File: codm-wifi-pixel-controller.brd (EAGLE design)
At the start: 59 x 25.5 mm, 24 parts, among them U1 ESP-WROOM-02, U2 AP2112K, U3 SN74AHCT125D

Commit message: development version 0.7
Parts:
- removed R3: 10k, rcl:R0805
- added C7, C8, C9: 2.2uF, rcl:C0603
- added U4: REG710NA-5/250, REG710NA-5_250:SOT95P280X145-6N
- C1, C2, C3, C4: device rcl:C0805 -> rcl:C0603
- C5: value 1u -> 1uF; device rcl:C0805 -> rcl:C0603
- C6: value 1u -> 2.2uF; device rcl:C0805 -> rcl:C0603
- F1: value 8V 500mA -> 24V 500mA (507-1803-1-ND)
- R1, R2: device rcl:R0805 -> rcl:R0603
- U2: value AP2112K -> TLV76733DRVR; device SparkFun-IC-Power:SOT23-5 -> TLV76733DRVR:SON65P200X200X80-7N
- moved C6 8.12 mm to (41.0, 3.00)
- moved C4 6.80 mm to (36.0, 17.2), turned to 0 degrees
- moved C5 6.73 mm to (47.0, 3.00), turned to 270 degrees
- moved RESET 2.07 mm to (32.3, 2.60)
- moved U$1 2.00 mm to (31.6, 21.8)
- moved U3 1.41 mm to (36.0, 11.5)
- moved D1 1.14 mm to (49.9, 9.60)
- moved JP1 1.00 mm to (20.8, 2.84)
- moved R1 1.00 mm to (41.4, 10.2)
- moved U$100 1.00 mm to (27.0, 9.50)
- moved U$2 1.00 mm to (8.00, 21.4)
- moved U1 1.00 mm to (20.8, 13.2)
- moved U2 0.71 mm to (44.0, 3.00)
- moved F1 0.64 mm to (49.9, 7.00)
- moved C3 0.57 mm to (8.60, 12.9)
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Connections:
- new net N$3: C9.2, U4.4
- new net VCCF: C5.1, D1.C, F1.2, U2.4, U2.6
- net +3V3: now also C6.2, C7.2, U2.1, U2.2, U4.3, U4.5; no longer C5.2, U2.5
- net +5V: now also C8.2, U4.1; no longer C6.2, D1.C, F1.2, R3.1, U2.1
- net GND: now also C5.2, C7.1, C8.1, U2.3, U2.5, U2.7, U4.2; no longer C5.1, U2.2
- net N$1: now also C9.1, U4.6; no longer R3.2, U2.3
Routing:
- net +5V: track 27.8 -> 10.7 mm
- net +3V3: track 60.9 -> 74.0 mm, vias 3 -> 9
- net VCCF: track 0.00 -> 7.05 mm, vias 0 -> 4
- net N$3: track 0.00 -> 5.27 mm
- net CLK-5V: track 23.1 -> 24.6 mm
- net DATA-5V: track 4.03 -> 3.13 mm
- net CHIPEN: track 13.6 -> 14.3 mm
- net CLK: track 32.4 -> 33.2 mm
- net N$1: track 2.35 -> 3.03 mm
- net STATLED: track 8.52 -> 7.93 mm
- net GND: vias 2 -> 15
- added copper zone on layer 1, net +3V3
- added copper zone on layer 16, net GND
- added copper zone on layer 1, net VCCF
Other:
- board text added: "4.7-16V"
- board text added: "90060-0.7"
- board text added: "VCC"
- board text added: "Wi-Fi Pixel Controller V0.7 codm.de 2021, CC-BY-NC-SA"
- board text added: "codm.de, 2021"
- board text removed: "+5V"
- board text removed: "90060-0.6"
- board text removed: "Wi-Fi Pixel Controller V0.6 codm.de 2020, CC-BY-NC-SA"
- board text removed: "codm.de, 2020"

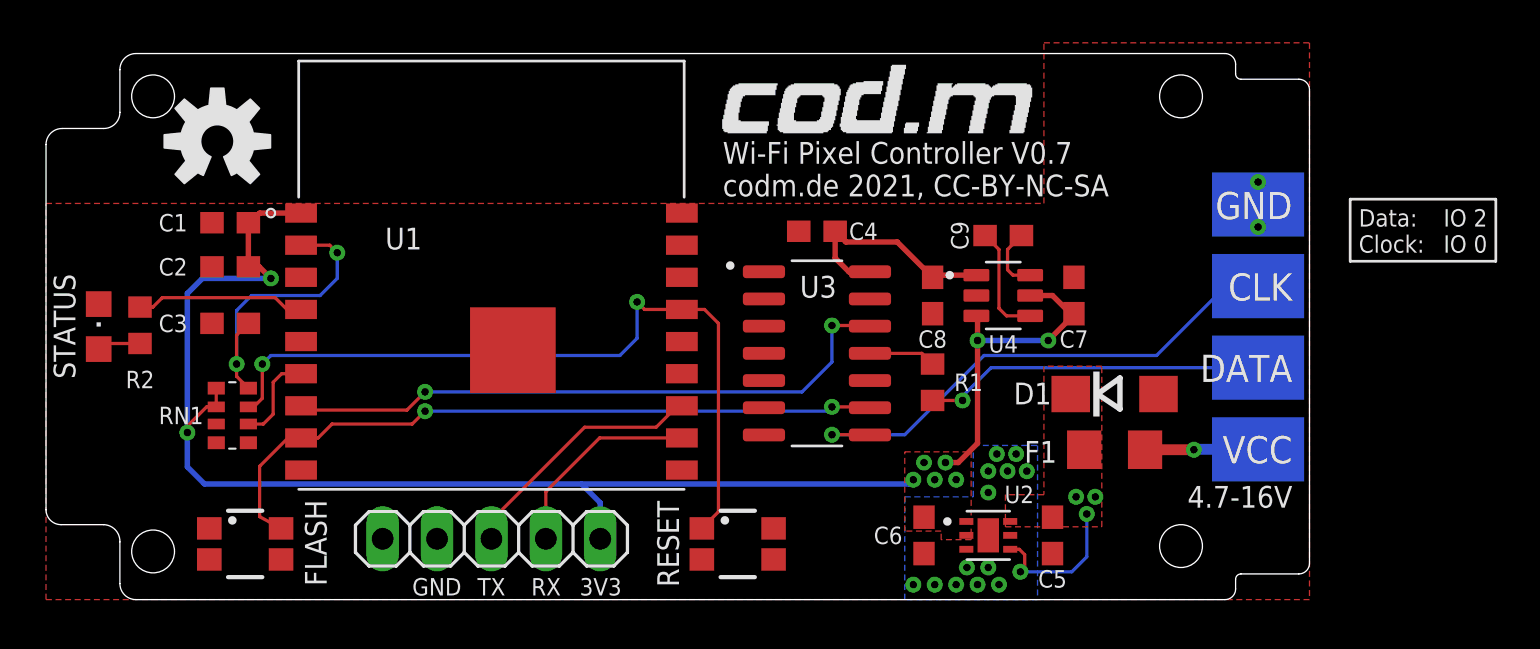
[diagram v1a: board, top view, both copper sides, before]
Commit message: version with TLV767 and bigger thermal via/planes
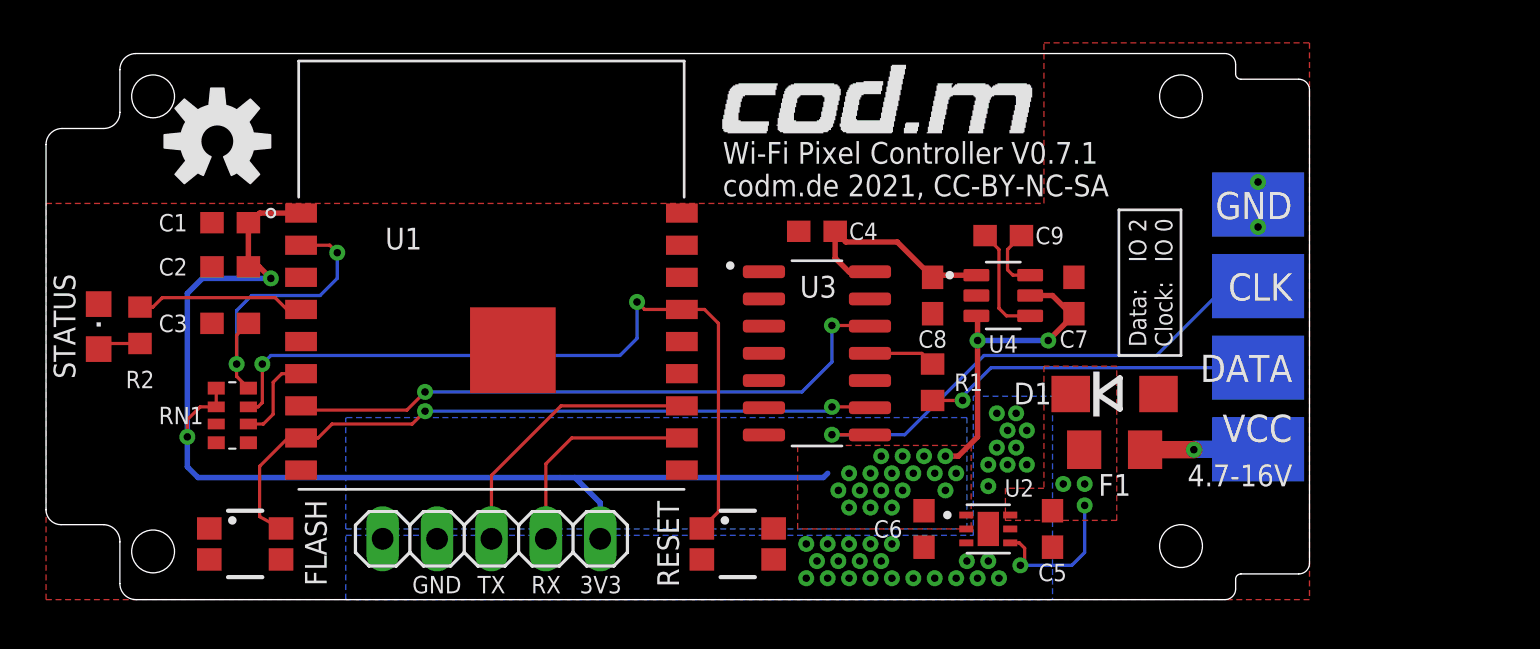
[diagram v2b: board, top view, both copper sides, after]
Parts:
- moved C5 0.30 mm to (47.0, 3.30)
- moved C6 0.30 mm to (41.0, 3.30)
- moved U2 0.30 mm to (44.0, 3.30)
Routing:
- net +3V3: track 74.0 -> 70.3 mm, vias 9 -> 22
- net TXD: track 12.0 -> 13.2 mm
- net RXD: track 9.59 -> 10.4 mm
- net GND: vias 15 -> 33
- added copper zone on layer 16, net +3V3
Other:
- board text added: "90060-0.7.1"
- board text added: "Wi-Fi Pixel Controller V0.7.1 codm.de 2021, CC-BY-NC-SA"
- board text removed: "90060-0.7"
- board text removed: "Wi-Fi Pixel Controller V0.7 codm.de 2021, CC-BY-NC-SA"

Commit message: prototype 0.7.2
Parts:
- added C10: 100n, rcl:C0603K
- added EN-2ND: (no value), jumper:SJ
- added R3: 330, rcl:R0603
- added TP1, TP2, TP3, TP4, TP5, TP6, TP7, TP8, TP9: PTR1TP14R, testpad:TP14R
- C1, C2, C3, C7, C8, C9: device rcl:C0603 -> rcl:C0603K
- C4: value 100n -> 10u; device rcl:C0603 -> rcl:C0805
- C5: value 1uF -> 10uF/16V; device rcl:C0603 -> rcl:C0805K
- C6: value 2.2uF -> 100n; device rcl:C0603 -> rcl:C0603K
- U2: value TLV76733DRVR -> TLV1117LV33DCYR; device TLV76733DRVR:SON65P200X200X80-7N -> TLV1117LV33DCYR:VREG_TLV1117LV33DCYR
- moved U$102 25.3 mm to (9.40, 19.5)
- moved U$100 24.7 mm to (50.3, 1.20)
- moved C4 9.20 mm to (34.1, 8.20)
- moved C6 7.48 mm to (34.1, 6.20), turned to 0 degrees
- moved C8 5.66 mm to (47.0, 15.0)
- moved U4 5.46 mm to (50.1, 15.0)
- moved C9 5.42 mm to (50.1, 17.5)
- moved C7 5.26 mm to (53.2, 15.0)
- moved R1 5.14 mm to (42.4, 15.2), turned to 180 degrees
- moved U3 3.10 mm to (35.9, 14.6), turned to 270 degrees
- moved U2 3.08 mm to (41.5, 5.10), turned to 180 degrees
- moved C5 1.87 mm to (47.5, 5.10)
- moved D1 1.17 mm to (50.3, 10.7)
- moved F1 1.17 mm to (50.3, 8.10)
- moved U$2 0.92 mm to (8.70, 20.8)
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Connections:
- net CLK-5V renamed CLK1-5V
- net DATA-5V renamed DATA1-5V
- new net CLK2-5V: TP9.TP, U3.3
- new net DATA2-5V: R3.2, U3.6
- new net DATA2-5VR: R3.1, TP8.TP
- new net IO13: TP5.TP, U1.5
- new net IO14: TP6.TP, U1.3
- new net IO16: U1.17, U3.2
- new net IO4: TP3.TP, U1.10
- new net IO5: TP4.TP, U1.14
- new net N$4: EN-2ND.2, U3.1, U3.4
- net +3V3: now also C4.2, TP2.TP, U2.4; no longer U2.1
- net +5V: now also C10.2; no longer C4.2
- net GND: now also C10.1, EN-2ND.1, TP1.TP, TP7.TP, U2.1; no longer U2.3, U2.5, U2.7, U3.1, U3.4
- net TXD: now also U3.5
- net VCCF: now also U2.3; no longer U2.4, U2.6
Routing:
- net +3V3: track 70.3 -> 37.0 mm, vias 22 -> 64
- net CLK2-5V: track 0.00 -> 16.1 mm, vias 0 -> 1
- net IO16: track 0.00 -> 14.6 mm, vias 0 -> 2
- net N$4: track 0.00 -> 12.7 mm, vias 0 -> 1
- net TXD: track 13.2 -> 24.5 mm
- net DATA2-5VR: track 0.00 -> 10.2 mm, vias 0 -> 1
- net DATA2-5V: track 0.00 -> 9.89 mm
- net IO4: track 0.00 -> 8.13 mm, vias 0 -> 1
- net GND: track 2.10 -> 9.44 mm, vias 33 -> 4
- net IO14: track 0.00 -> 4.69 mm, vias 0 -> 1
- net DATA1-5V: track 3.13 -> 7.80 mm
- net IO5: track 0.00 -> 4.12 mm, vias 0 -> 1
- net IO13: track 0.00 -> 4.03 mm, vias 0 -> 1
- net CLK: track 33.2 -> 30.3 mm
- net DATA-5VR: track 16.0 -> 18.7 mm
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- removed copper zone on layer 16, net GND
- removed copper zone on layer 1, net VCCF
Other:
- board text added: "3.3V"
- board text added: "90060-0.7.2"
- board text added: "Clock-2 (IO16)"
- board text added: "Data-2 (IO1)"
- board text added: "IO13"
- board text added: "IO14"
- board text added: "IO4"
- board text added: "IO5"
- board text added: "Wi-Fi Pixel Controller V0.7.2 codm.de 2021, CC-BY-NC-SA"
- board text removed: "90060-0.7.1"
- board text removed: "Thank you for the idea, Dennis. www.unser-smartes-zuhause.de"
- board text removed: "Wi-Fi Pixel Controller V0.7.1 codm.de 2021, CC-BY-NC-SA"

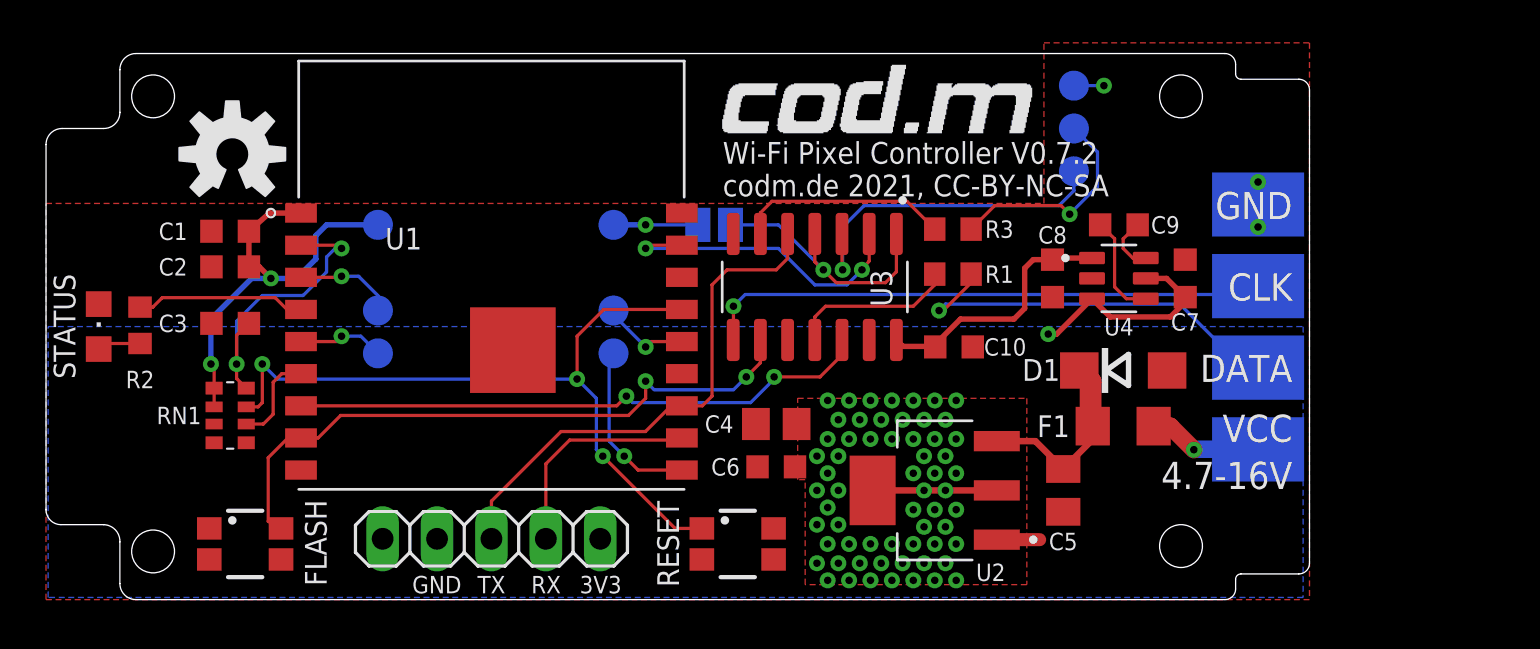
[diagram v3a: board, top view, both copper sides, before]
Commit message: V0.7.3 - forgot reverse polarity protection
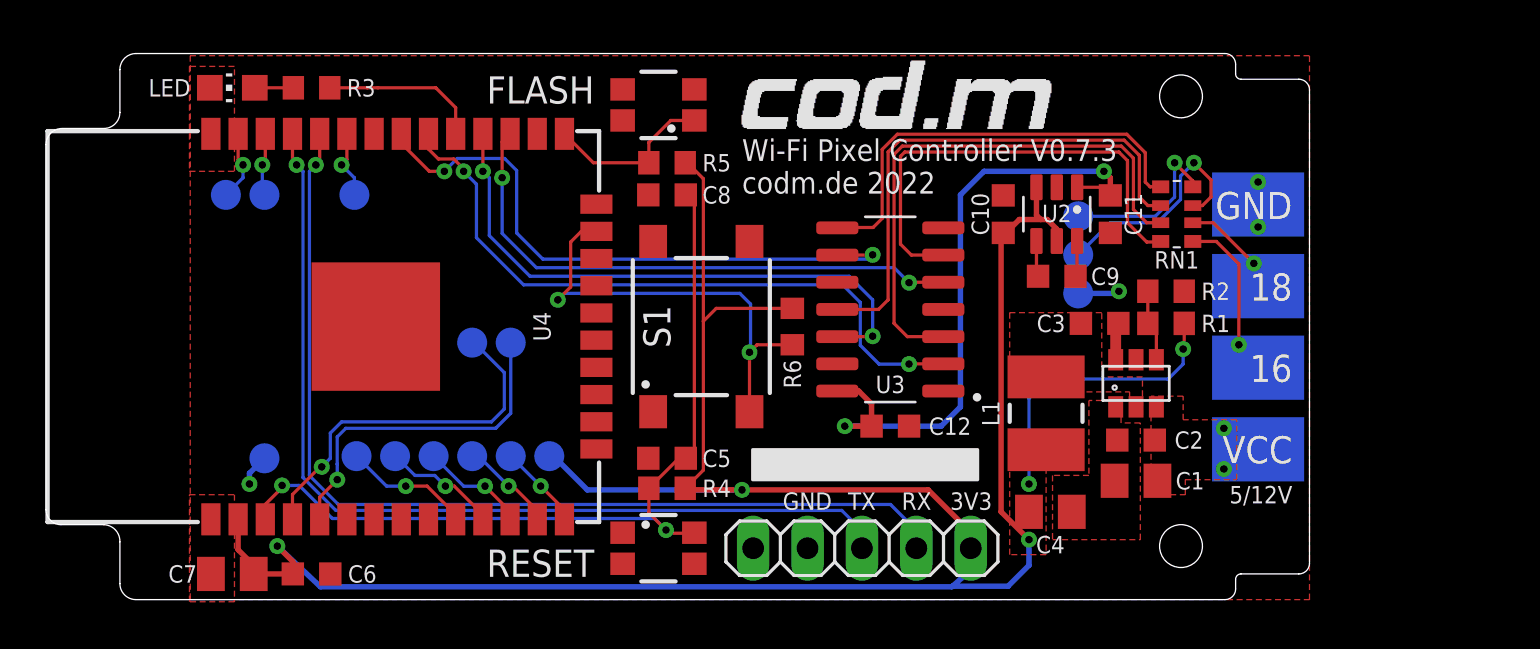
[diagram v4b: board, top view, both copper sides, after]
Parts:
- removed D1: SK34A, diode:DO214AC
- removed EN-2ND: (no value), jumper:SJ
- removed F1: 24V 500mA (507-1803-1-ND), adafruit:R1206
- removed STATUS: (no value), led:CHIPLED_0805
- removed U$2: (no value), SparkFun-Aesthetics:OSHW-LOGO-M
- added C11: 2.2uF, rcl:C0603K
- added C12: 100n, rcl:C0603K
- added L1: 3.3uH, Eagle_WE-LQ (rev19a):WE-LQ_1812
- added LED: 150080RS75000, led:CHIP-LED0805
- added R4, R5, R6: 10k, rcl:R0603
- added S1: 430182070816, Eagle_WS-TASV (rev21c):430182070816
- added TP10, TP11, TP12, TP13, TP14, TP15: PTR1TP14R, testpad:TP14R
- C1: value 100n -> 10u; device rcl:C0603K -> rcl:C0805K
- C10: value 100n -> 2.2uF
- C2: value 10µ -> 100n
- C4: value 10u -> 22uF/6.3V/20%; device rcl:C0805 -> rcl:C0805K
- C5: value 10uF/16V -> 1u; device rcl:C0805K -> rcl:C0603K
- C7: value 2.2uF -> 22uF/6.3V/20%; device rcl:C0603K -> rcl:C0805K
- C8: value 2.2uF -> 100n
- R1: value 330 -> 69k8
- R2: value 2k7 -> 22k1
- R3: value 330 -> 2k7
- RN1: value 10k -> 330
- U1: value ESP-WROOM-02 -> AP62XXX-TSOT26; device ESP-WROOM-02:MODULE_ESP-WROOM-02 -> codm:AP62XXX-TSOT26
- U2: value TLV1117LV33DCYR -> REG710NA-5/250; device TLV1117LV33DCYR:VREG_TLV1117LV33DCYR -> REG710NA-5_250:SOT95P280X145-6N
- U4: value REG710NA-5/250 -> ESP-WROOM-32; device REG710NA-5_250:SOT95P280X145-6N -> esp32:ESP-WROOM-32
- moved R2 47.9 mm to (52.3, 14.4), turned to 0 degrees
- moved C7 46.6 mm to (8.70, 1.20), turned to 0 degrees
- moved RN1 45.2 mm to (52.8, 18.0)
- moved C1 43.9 mm to (50.9, 5.55), turned to 0 degrees
- moved C2 43.1 mm to (50.9, 7.45)
- moved C3 40.6 mm to (49.2, 12.9)
- moved U4 34.8 mm to (15.4, 12.8), turned to 180 degrees
- moved R3 30.7 mm to (12.4, 23.9), turned to 0 degrees
- moved U1 30.3 mm to (50.9, 10.1), turned to 90 degrees
- moved FLASH 28.2 mm to (28.6, 23.1), turned to 180 degrees
- moved C6 22.3 mm to (12.4, 1.20)
- moved TP1 19.6 mm to (10.2, 6.60)
- moved U$102 19.1 mm to (27.2, 12.7)
- moved C5 18.6 mm to (29.0, 6.60), turned to 180 degrees
- moved C8 18.4 mm to (29.0, 18.9), turned to 0 degrees
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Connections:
- removed net BOOTMODE: RN1.2, U1.6
- removed net CHIPEN: C3.1, RN1.4, U1.2
- removed net CLK: FLASH.3, U1.8, U3.9
- removed net CLK1-5V: U$101.P$2, U3.8
- removed net CLK2-5V: TP9.TP, U3.3
- removed net DATA: U1.7, U3.12
- removed net DATA-5VR: R1.1, U$101.P$3
- removed net DATA1-5V: R1.2, U3.11
- removed net DATA2-5V: R3.2, U3.6
- removed net DATA2-5VR: R3.1, TP8.TP
- removed net IO13: TP5.TP, U1.5
- removed net IO4: TP3.TP, U1.10
- removed net IO5: TP4.TP, U1.14
- removed net N$1: C9.1, U4.6
- removed net N$2: R2.1, STATUS.A
- removed net N$3: C9.2, U4.4
- removed net N$4: EN-2ND.2, U3.1, U3.4
- removed net RST: RESET.1, RN1.3, U1.15
- removed net STATLED: R2.2, U1.4
- removed net VCCF: C5.1, D1.C, F1.2, U2.3
- new net BST: C3.1, U1.BST
- new net BTN: R6.2, S1.2, U4.23
- new net GPIO0: FLASH.1, R5.2, U4.25
- new net IO12: TP3.TP, U4.14
- new net IO16-5V: RN1.8, U3.6
- new net IO16-5VR: RN1.1, U$101.P$3
- new net IO17: U3.12, U4.28
- new net IO17-5V: RN1.6, U3.11
- new net IO17-5VR: RN1.3, TP8.TP
- new net IO18: U3.2, U4.30
- new net IO18-5V: RN1.7, U3.3
- new net IO18-5VR: RN1.2, U$101.P$2
- new net IO19: U3.9, U4.31
- new net IO19-5V: RN1.5, U3.8
- new net IO19-5VR: RN1.4, TP9.TP
- new net IO21: TP13.TP, U4.33
- new net IO22: TP12.TP, U4.36
- new net IO23: TP11.TP, U4.37
- new net IO25: TP10.TP, U4.10
- new net IO26: TP6.TP, U4.11
- new net IO27: TP5.TP, U4.12
- new net N$5: C9.1, U2.6
- new net N$6: R1.2, R2.1, U1.FB
- new net N$7: LED.A, R3.1
- new net N$8: C9.2, U2.4
- new net RESET: C5.1, C8.2, R4.1, RESET.3, U4.3
- new net STATUS-LED: R3.2, U4.29
- new net SW: C3.2, L1.1, U1.SW
- new net S_VN: TP14.TP, U4.5
- new net S_VP: TP15.TP, U4.4
- net +3V3: now also C10.2, C4.1, C6.1, L1.2, R1.1, R4.2, R5.1, R6.1, U2.3, U2.5, U4.2; no longer C1.1, C2.1, C4.2, C6.2, RN1.5, RN1.6, U1.1, U2.2, U2.4, U4.3, U4.5
- net +5V: now also C11.2, C12.2, U2.1; no longer C10.2, C8.2, U4.1
- net GND: now also C1.1, C11.1, C12.1, C4.2, C6.2, FLASH.3, LED.C, R2.2, RESET.1, S1.1, U1.GND, U2.2, U3.1, U3.4, U4.1, U4.15, U4.38, U4.GND; no longer C1.2, C3.2, C4.1, C6.1, D1.A, EN-2ND.1, FLASH.4, RESET.2, RN1.7, STATUS.C, U1.13, U1.18, U1.19, U1.9, U2.1, U4.2
- net IO14: now also TP4.TP, U4.13; no longer TP6.TP, U1.3
- net IO16: now also U3.5, U4.27; no longer U1.17, U3.2
- net RXD: now also U4.34; no longer U1.11
- net TXD: now also U4.35; no longer U1.12, U3.5
- net VCC: now also C1.2, C2.1, U1.VIN; no longer F1.1
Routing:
- net +3V3: track 37.0 -> 124.5 mm, vias 64 -> 5
- net RESET: track 0.00 -> 39.3 mm, vias 0 -> 2
- net RXD: track 10.4 -> 46.4 mm, vias 0 -> 1
- net RST: track 35.2 -> 0.00 mm, vias 3 -> 0
- net IO18: track 0.00 -> 31.6 mm, vias 0 -> 2
- net CLK: track 30.3 -> 0.00 mm, vias 2 -> 0
- net IO19: track 0.00 -> 28.6 mm, vias 0 -> 2
- net IO17: track 0.00 -> 27.4 mm, vias 0 -> 2
- net DATA: track 27.3 -> 0.00 mm, vias 2 -> 0
- net CLK1-5V: track 26.5 -> 0.00 mm, vias 1 -> 0
- net IO18-5V: track 0.00 -> 25.9 mm
- net IO17-5V: track 0.00 -> 24.8 mm
- net IO16-5V: track 0.00 -> 22.0 mm
- net BTN: track 0.00 -> 20.9 mm, vias 0 -> 2
- net IO19-5V: track 0.00 -> 20.6 mm
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- added copper zone on layer 1, net SW
- added copper zone on layer 1, net VCC
- removed copper zone on layer 16, net +3V3
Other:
- board text added: "16"
- board text added: "18"
- board text added: "5/12V"
- board text added: "90060-0.7.3"
- board text added: "IO12"
- board text added: "IO17@5V,8mA"
- board text added: "IO19@5V,8mA"
- board text added: "IO21"
- board text added: "IO22"
- board text added: "IO23"
- board text added: "IO25"
- board text added: "IO26"
- board text added: "IO27"
- board text added: "S_VN"
- board text added: "S_VP"
- board text added: "Wi-Fi Pixel Controller V0.7.3 codm.de 2022"
- board text added: "Wi-Fi Pixel Controller V0.7.3 codm.de, 2022 CC-BY-NC-SA"
- board text removed: "4.7-16V"
- board text removed: "90060-0.7.2"
- board text removed: "CLK"
- board text removed: "Clock-2 (IO16)"
- board text removed: "DATA"
- board text removed: "Data-2 (IO1)"
- board text removed: "Data: Clock:"
- board text removed: "IO 2 IO 0"
- board text removed: "IO13"
- board text removed: "IO4"
- board text removed: "IO5"
- board text removed: "Wi-Fi Pixel Controller V0.7.2 codm.de 2021, CC-BY-NC-SA"
- board text removed: "codm.de, 2021"
